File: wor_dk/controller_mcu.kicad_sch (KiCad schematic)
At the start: 46 parts, among them J401 USB_A, J402 Prog, SW401 SW_Push, SW402 SW_Push, U401 nRF52840, Y401 32MHz

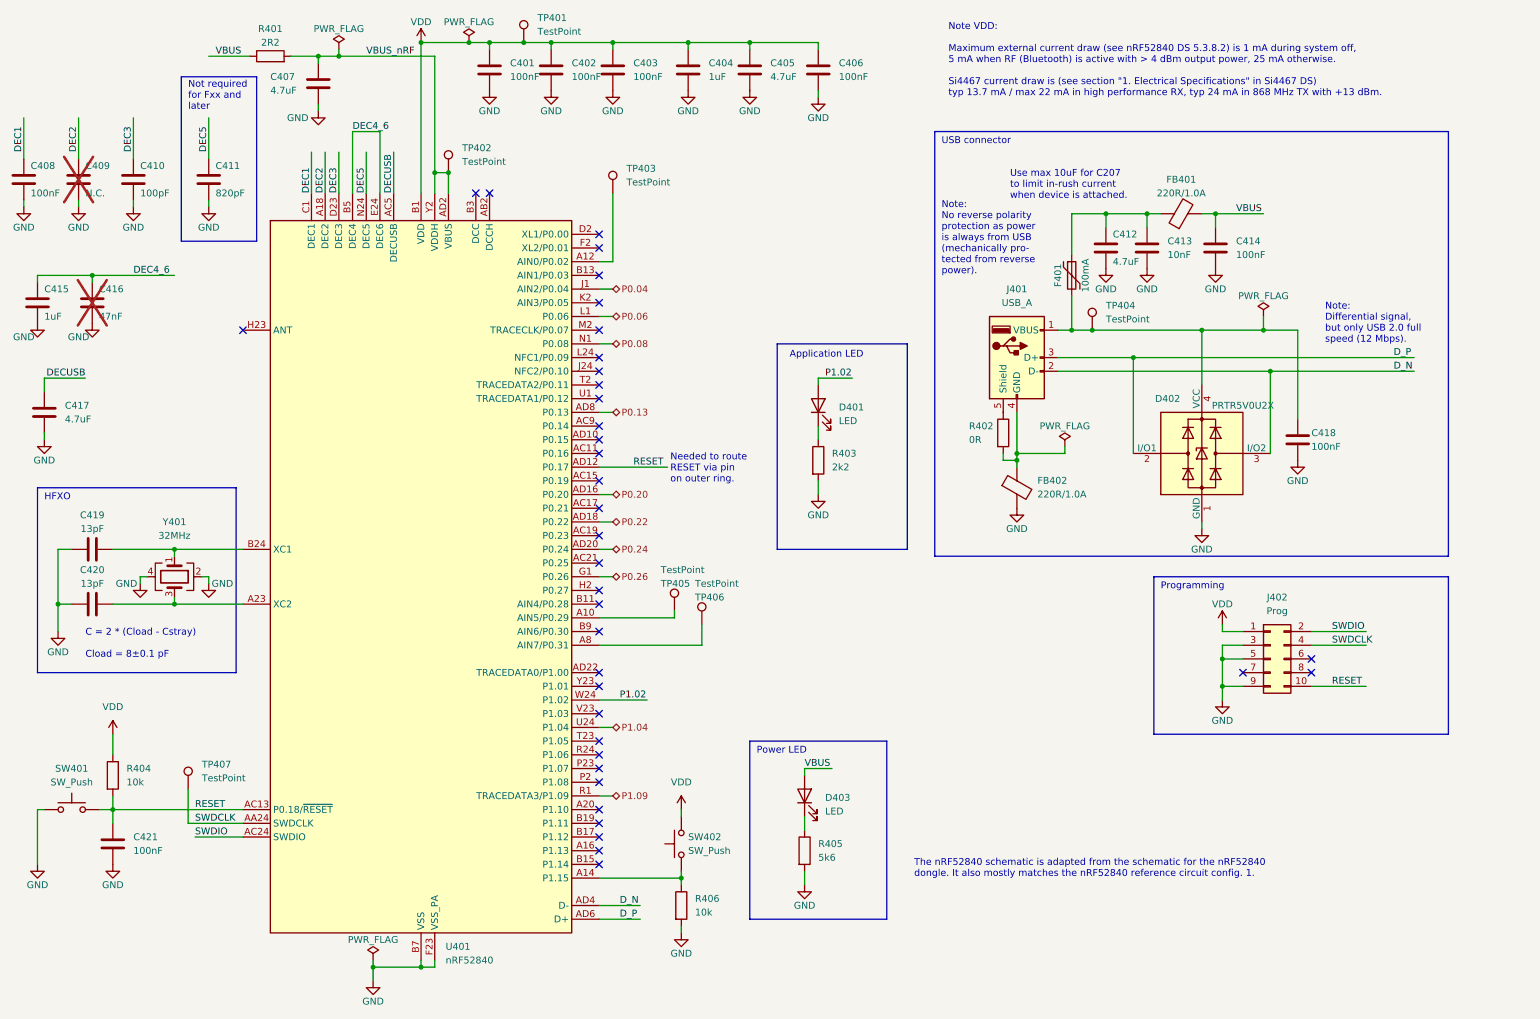
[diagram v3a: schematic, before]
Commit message: wor_dk: schematic: add multiplexers for programmer & GPIO
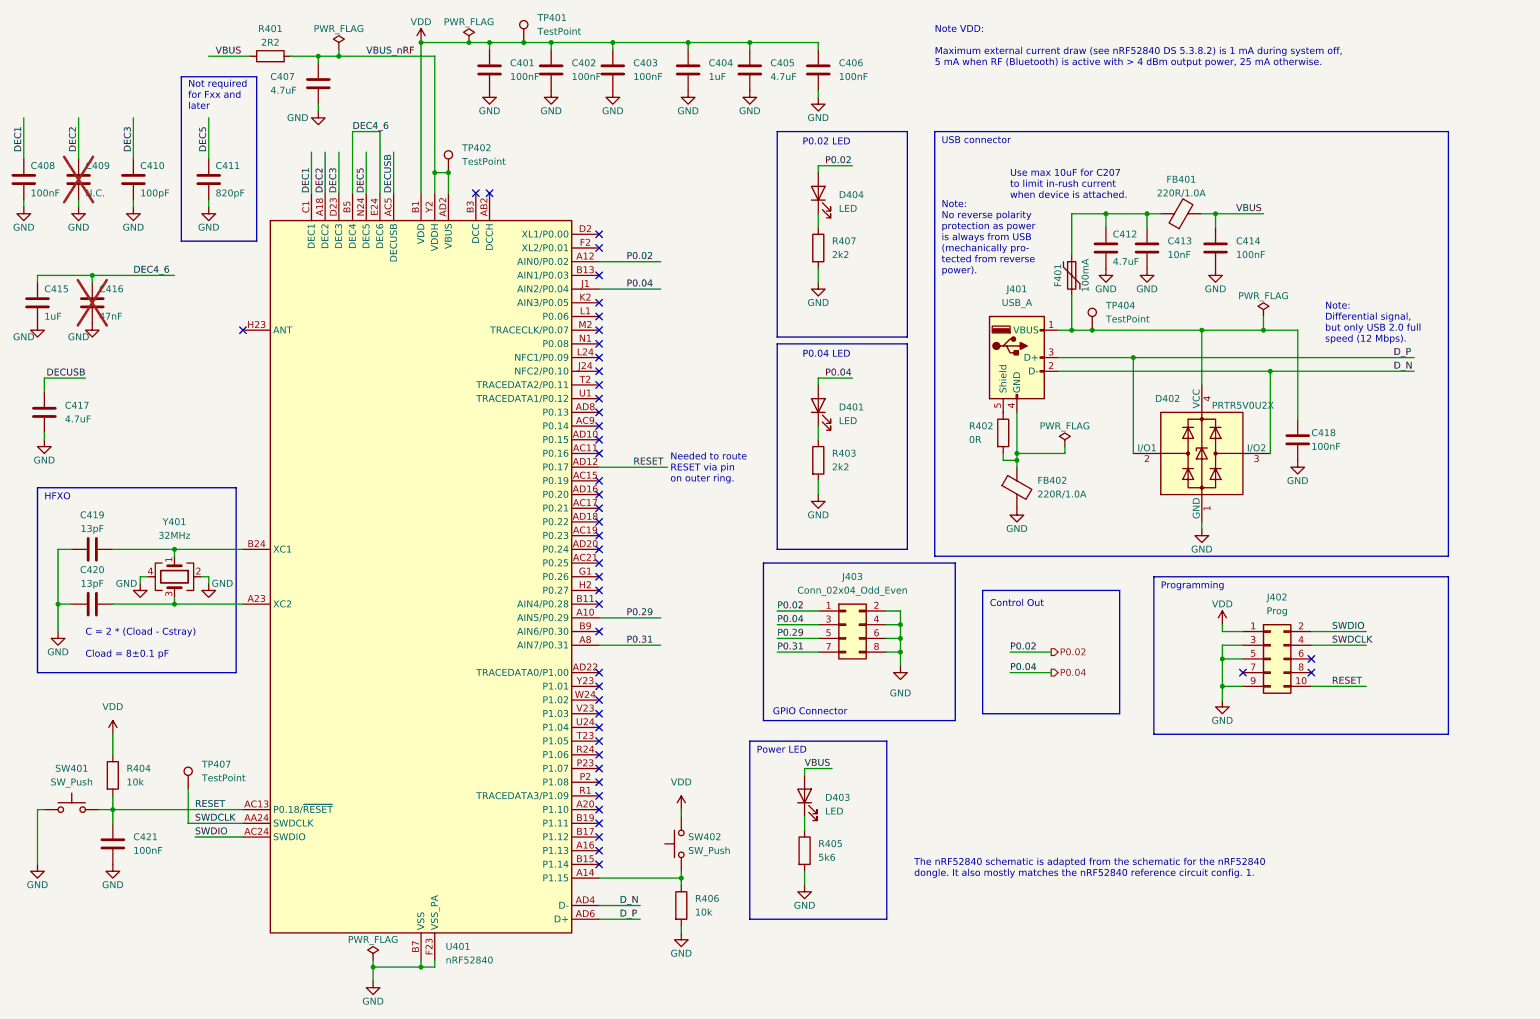
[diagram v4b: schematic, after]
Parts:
- removed TP403, TP405, TP406: TestPoint, TestPoint:TestPoint_Pad_D1.0mm, symbol Connector:TestPoint
- added D404: LED, LED_SMD:LED_0805_2012Metric, symbol Device:LED
- added J403: Conn_02x04_Odd_Even, symbol Connector_Generic:Conn_02x04_Odd_Even
- added R407: 2k2, Resistor_SMD:R_0402_1005Metric, symbol Device:R
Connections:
- net GND: now also J403.2 (Pin_2), J403.4 (Pin_4), J403.6 (Pin_6), J403.8 (Pin_8), R407.2
- net P0.04: now also D401.2 (A), J403.3 (Pin_3)
- net P0.31: now reaches U401.A8 (AIN7/P0.31)
- net P0.31: now also J403.7 (Pin_7)
- net P0.02: now reaches U401.A12 (AIN0/P0.02)
- net P0.02: now also D404.2 (A), J403.1 (Pin_1)
- net P0.29: now reaches U401.A10 (AIN5/P0.29)
- net P0.29: now also J403.5 (Pin_5)
- net P0.06: no longer names the net of U401.L1 (P0.06)
- net P0.08: no longer names the net of U401.N1 (P0.08)
- net P0.13: no longer names the net of U401.AD8 (P0.13)
- net P0.20: no longer names the net of U401.AD16 (P0.20)
- net P0.22: no longer names the net of U401.AD18 (P0.22)
- net P0.24: no longer names the net of U401.AD20 (P0.24)
- net P0.26: no longer names the net of U401.G1 (P0.26)
- net P1.02: no longer names the net of U401.W24 (P1.02)
- net P1.02: no longer D401.2 (A)
- net P1.04: no longer names the net of U401.U24 (P1.04)
- net P1.09: no longer names the net of U401.R1 (TRACEDATA3/P1.09)
- new net: D404.1 (K), R407.1
- no-connect marks 37 -> 47
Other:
- note added: "Control Out"
- note added: "GPIO Connector"
- note added: "Note VDD: Maximum external current draw (see nRF52840 DS 5.3.8.2) is 1 mA during system off, 5 mA when RF (Bluetooth) is active with > 4 dBm output power, 25 mA otherwise."
- note added: "P0.02 LED"
- note added: "P0.04 LED"
- note removed: "Application LED"
- note removed: "Note VDD: Maximum external current draw (see nRF52840 DS 5.3.8.2) is 1 mA during system off, 5 mA when RF (Bluetooth) is active with > 4 dBm output power, 25 mA otherwise. Si4467 current draw is (see section "1. Electrical Specifications" in Si4467 DS) typ 13.7 mA / max 22 mA in high performance RX, typ 24 mA in 868 MHz TX with +13 dBm."

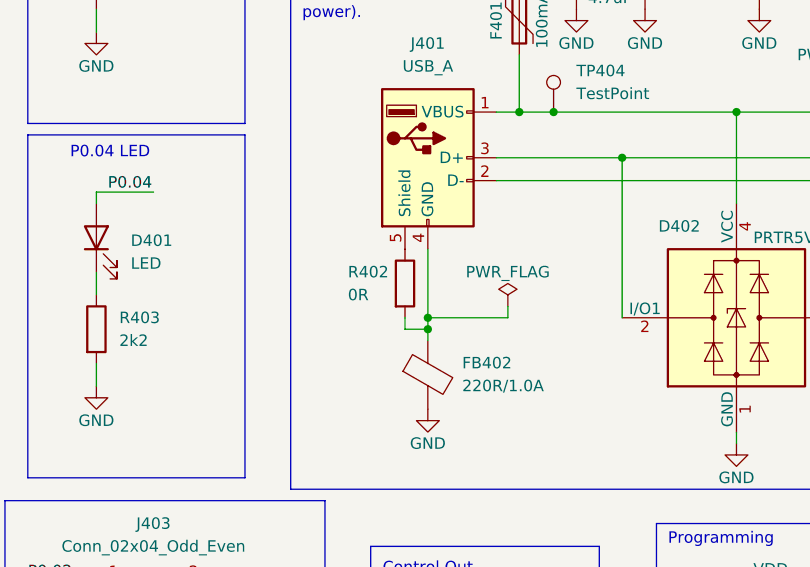
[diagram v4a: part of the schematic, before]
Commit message: wor_dk: add programmer
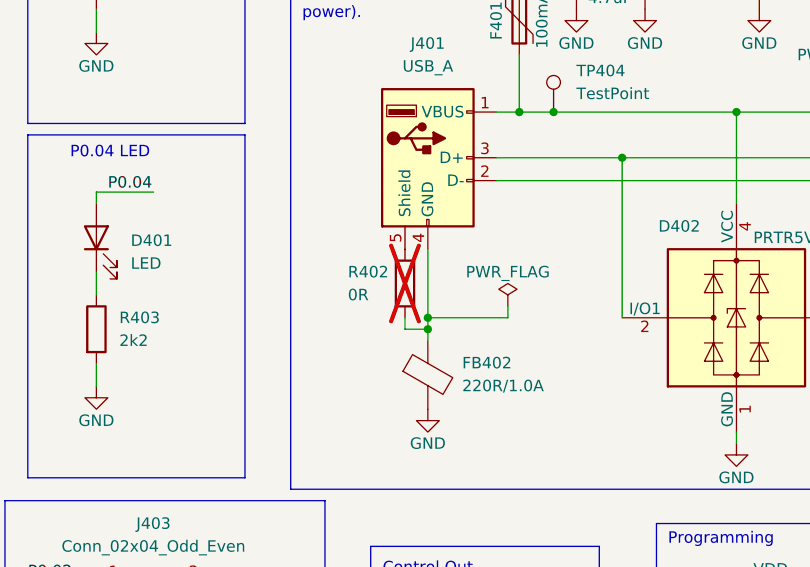
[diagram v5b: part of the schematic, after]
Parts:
- R402: now not fitted
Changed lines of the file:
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@@
 		(in_bom yes)
 		(on_board yes)
-		(dnp no)
+		(dnp yes)
 		(property "Reference" "R402"
 			(at 190.5 90.17 0)
